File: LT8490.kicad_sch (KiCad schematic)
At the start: 81 parts

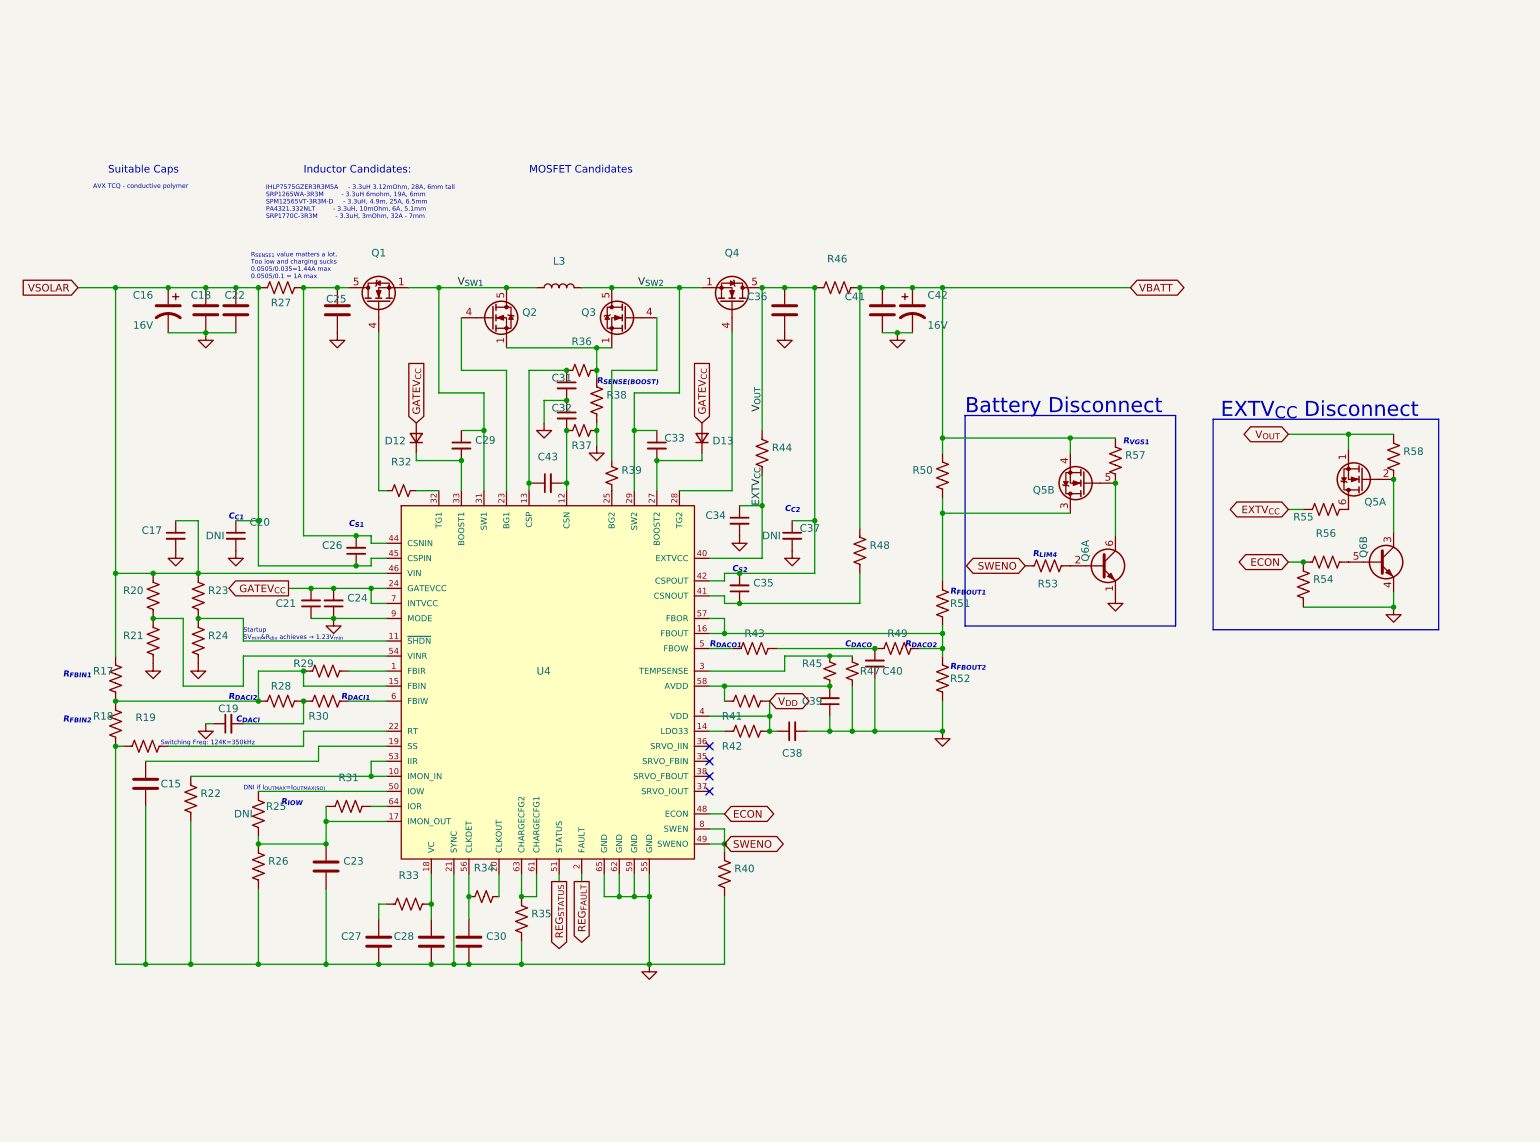
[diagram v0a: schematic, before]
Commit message: routed on 6 layers. Possible to do 4?
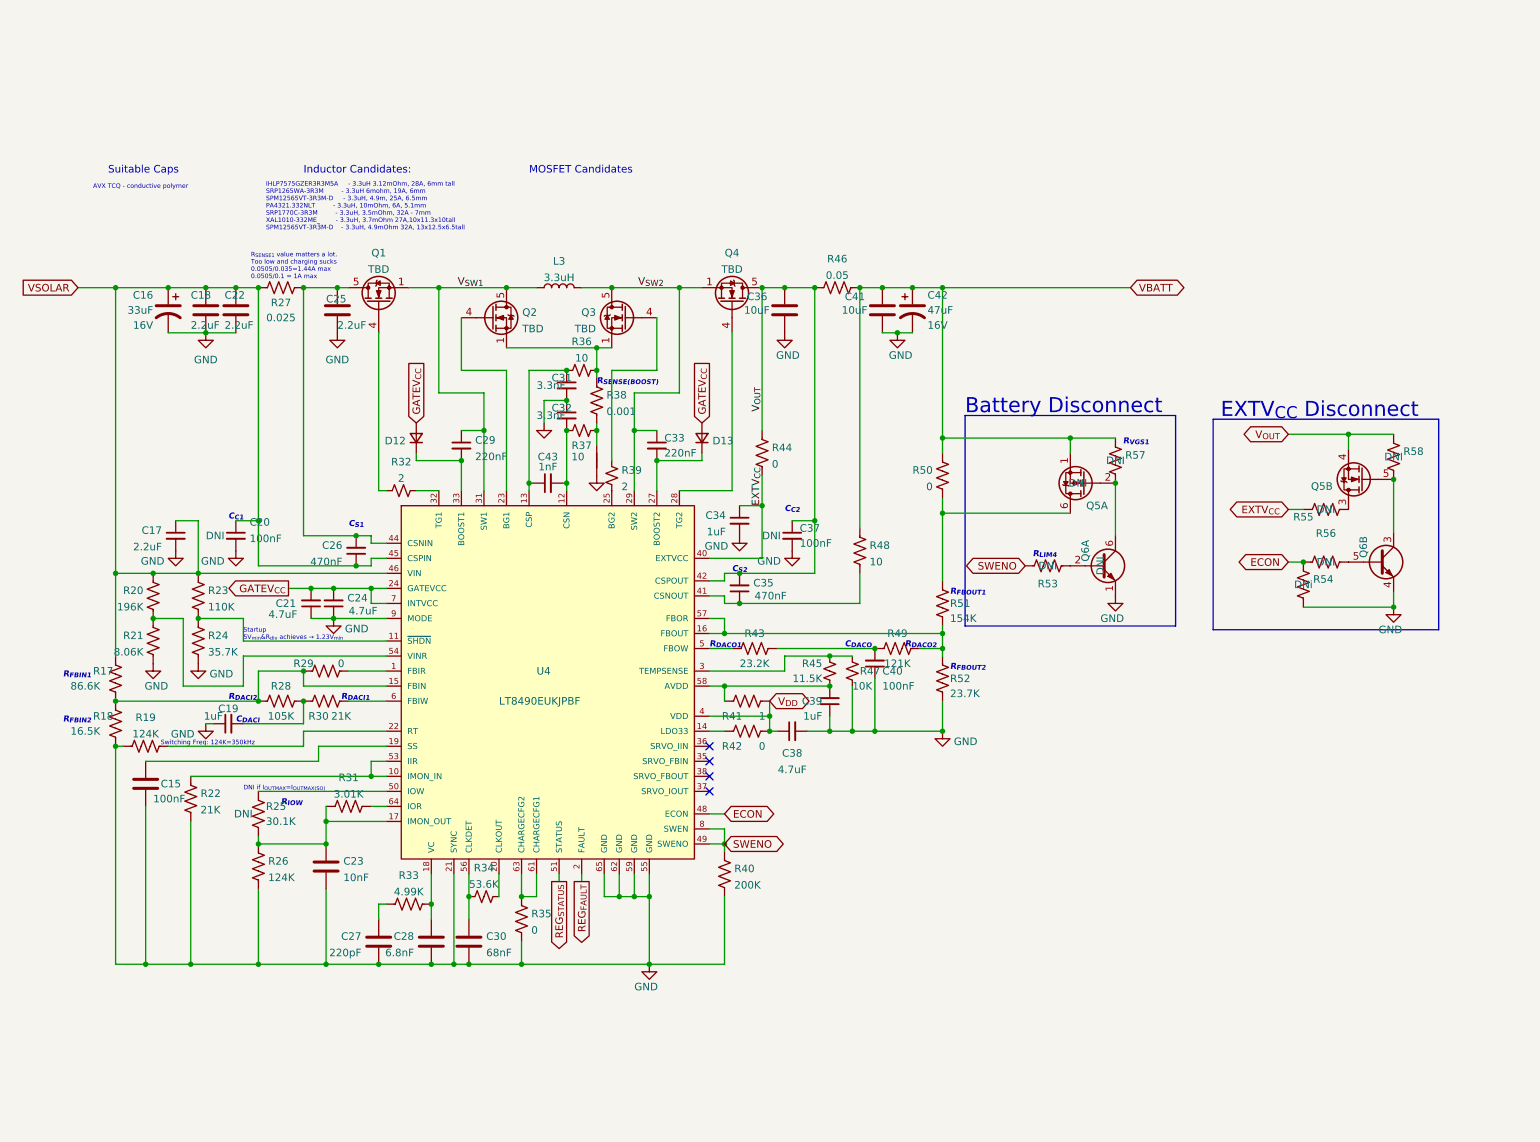
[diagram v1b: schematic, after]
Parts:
- added NT1: NetTie_2, NetTie:NetTie-2_SMD_Pad0.5mm, symbol Device:NetTie_2
- C15, C20, C37, C40: value (none) -> 100nF; footprint (none) -> Capacitor_SMD:C_0603_1608Metric
- C16: value (none) -> 33uF; footprint (none) -> Capacitor_Tantalum_SMD:CP_EIA-7343-30_AVX-N
- C17: value (none) -> 2.2uF; footprint (none) -> Capacitor_SMD:C_0603_1608Metric
- C18, C22, C25: value (none) -> 2.2uF; footprint (none) -> Capacitor_SMD:C_0805_2012Metric
- C19, C34, C39: value (none) -> 1uF; footprint (none) -> Capacitor_SMD:C_0603_1608Metric
- C21, C24, C38: value (none) -> 4.7uF; footprint (none) -> Capacitor_SMD:C_0603_1608Metric
- C23: value (none) -> 10nF; footprint (none) -> Capacitor_SMD:C_0603_1608Metric
- C26, C35: value (none) -> 470nF; footprint (none) -> Capacitor_SMD:C_0603_1608Metric
- C27: value (none) -> 220pF; footprint (none) -> Capacitor_SMD:C_0603_1608Metric
- C28: value (none) -> 6.8nF; footprint (none) -> Capacitor_SMD:C_0603_1608Metric
- C29, C33: value (none) -> 220nF; footprint (none) -> Capacitor_SMD:C_0603_1608Metric
- C30: value (none) -> 68nF; footprint (none) -> Capacitor_SMD:C_0603_1608Metric
- C31, C32: value (none) -> 3.3nF; footprint (none) -> Capacitor_SMD:C_0603_1608Metric
- C36, C41: value (none) -> 10uF; footprint (none) -> Capacitor_SMD:C_0805_2012Metric
- C42: value (none) -> 47uF; footprint (none) -> Capacitor_Tantalum_SMD:CP_EIA-7343-30_AVX-N
- C43: value (none) -> 1nF; footprint (none) -> Capacitor_SMD:C_0603_1608Metric
- D12, D13: value (none) -> DFLS130L; footprint (none) -> Diode_SMD:D_PowerDI-123
- L3: value (none) -> 3.3uH; footprint (none) -> custom-footprints:L_IHLP7575
- Q1, Q2, Q3, Q4: value (none) -> TBD; footprint (none) -> Package_SO:PowerPAK_SO-8_Single
- Q5, Q6, R53, R55, R56, R57, R58: DNI (none) -> DNI
- R17: value (none) -> 86.6K; footprint (none) -> Resistor_SMD:R_0603_1608Metric
- R18: value (none) -> 16.5K; footprint (none) -> Resistor_SMD:R_0603_1608Metric
- R19, R26: value (none) -> 124K; footprint (none) -> Resistor_SMD:R_0603_1608Metric
- R20: value (none) -> 196K; footprint (none) -> Resistor_SMD:R_0603_1608Metric
- R21: value (none) -> 8.06K; footprint (none) -> Resistor_SMD:R_0603_1608Metric
- R22, R30: value (none) -> 21K; footprint (none) -> Resistor_SMD:R_0603_1608Metric
- R23: value (none) -> 110K; footprint (none) -> Resistor_SMD:R_0603_1608Metric
- R24: value (none) -> 35.7K; footprint (none) -> Resistor_SMD:R_0603_1608Metric
- R25: value (none) -> 30.1K; footprint (none) -> Resistor_SMD:R_0603_1608Metric
- R27: value (none) -> 0.025; footprint (none) -> Resistor_SMD:R_1206_3216Metric
- R28: value (none) -> 105K; footprint (none) -> Resistor_SMD:R_0603_1608Metric
- R29, R35, R42, R44, R50: value (none) -> 0; footprint (none) -> Resistor_SMD:R_0603_1608Metric
- R31: value (none) -> 3.01K; footprint (none) -> Resistor_SMD:R_0603_1608Metric
- R32, R39: value (none) -> 2; footprint (none) -> Resistor_SMD:R_0603_1608Metric
- R33: value (none) -> 4.99K; footprint (none) -> Resistor_SMD:R_0603_1608Metric
- R34: value (none) -> 53.6K; footprint (none) -> Resistor_SMD:R_0603_1608Metric
- R36, R37, R48: value (none) -> 10; footprint (none) -> Resistor_SMD:R_0603_1608Metric
- R38: value (none) -> 0.001; footprint (none) -> Resistor_SMD:R_1206_3216Metric
- R40: value (none) -> 200K; footprint (none) -> Resistor_SMD:R_0603_1608Metric
- R41: value (none) -> 1; footprint (none) -> Resistor_SMD:R_0603_1608Metric
- R43: value (none) -> 23.2K; footprint (none) -> Resistor_SMD:R_0603_1608Metric
- R45: value (none) -> 11.5K; footprint (none) -> Resistor_SMD:R_0603_1608Metric
- R46: value (none) -> 0.05; footprint (none) -> Resistor_SMD:R_1206_3216Metric
- R47: value (none) -> 10K; footprint (none) -> Resistor_SMD:R_0603_1608Metric
- R49: value (none) -> 121K; footprint (none) -> Resistor_SMD:R_0603_1608Metric
- R51: value (none) -> 154K; footprint (none) -> Resistor_SMD:R_0603_1608Metric
- R52: value (none) -> 23.7K; footprint (none) -> Resistor_SMD:R_0603_1608Metric
- R54: DNI (none) -> DNi
- U4: value (none) -> LT8490EUKJPBF; footprint (none) -> custom-footprints:LT8490EUKJ#PBF
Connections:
- net GND: now also NT1.1; no longer R37.1, R38.2
- net VBATT: now also Q5.1 (S2); no longer Q5.4 (S1)
- net V_{OUT}: now also Q5.4 (S1); no longer Q5.1 (S2)
- net at Q6.3 (C2), R58.1: now also Q5.5 (G1); no longer Q5.2 (G2)
- net at R50.2, R51.1: now also Q5.6 (D1); no longer Q5.3 (D2)
- net at R55.1: now also Q5.3 (D2); no longer Q5.6 (D1)
- net at Q6.6 (C1), R57.1: now also Q5.2 (G2); no longer Q5.5 (G1)
- new net: NT1.2, R37.1, R38.2
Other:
- note added: "IHLP7575GZER3R3M5A - 3.3uH 3.12mOhm, 28A, 6mm tall SRP1265WA-3R3M - 3.3uH 6mohm, 19A, 6mm SPM12565VT-3R3M-D - 3.3uH, 4.9m, 25A, 6.5mm PA4321.332NLT - 3.3uH, 10mOhm, 6A, 5.1mm SRP1770C-3R3M - 3.3uH, 3.5mOhm, 32A - 7mm XAL1010-332ME_ - 3.3uH, 3.7mOhm 27A,10x11.3x10tall SPM12565VT-3R3M-D - 3.3uH, 4.9mOhm 32A, 13x12.5x6.5tall"
- note removed: "IHLP7575GZER3R3M5A - 3.3uH 3.12mOhm, 28A, 6mm tall SRP1265WA-3R3M - 3.3uH 6mohm, 19A, 6mm SPM12565VT-3R3M-D - 3.3uH, 4.9m, 25A, 6.5mm PA4321.332NLT - 3.3uH, 10mOhm, 6A, 5.1mm SRP1770C-3R3M - 3.3uH, 3mOhm, 32A - 7mm"
- moved on the sheet: Q5A, Q5B

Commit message: evaluating layout for sensitive signals
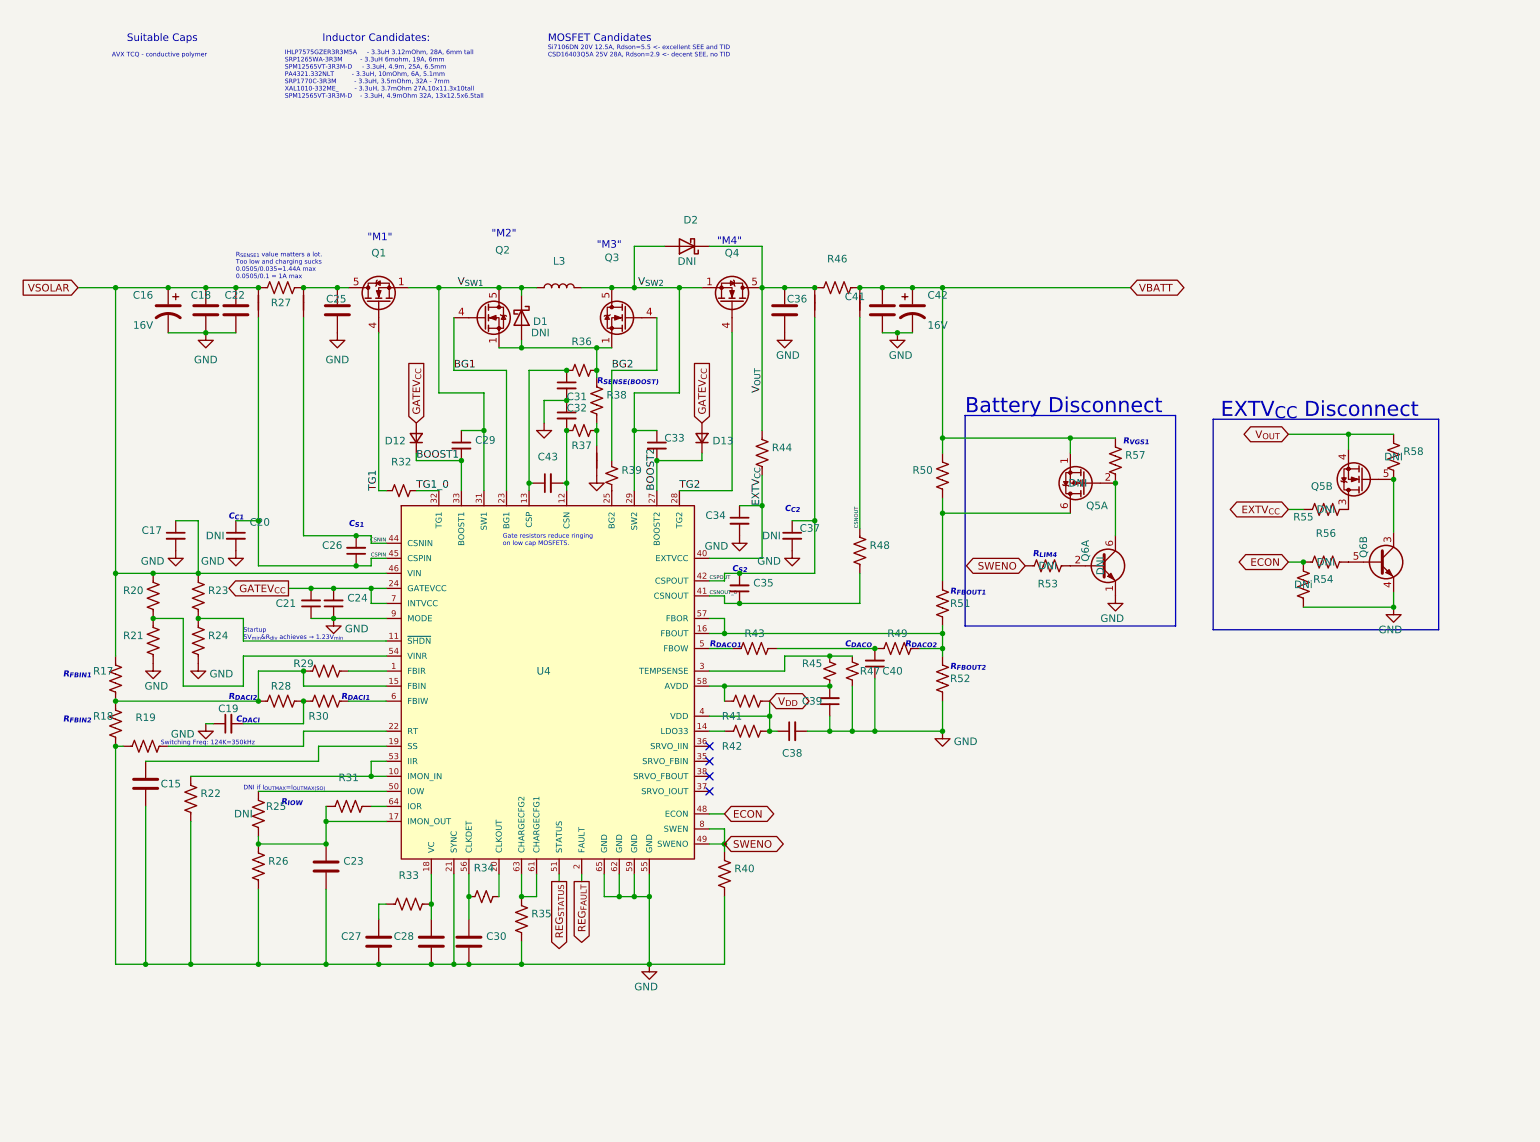
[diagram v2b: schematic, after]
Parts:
- added D1, D2: (no value), symbol Device:D_Schottky
- added NT2, NT3, NT4, NT5: NetTie_2, NetTie:NetTie-2_SMD_Pad0.5mm, symbol Device:NetTie_2
- C15, C20, C37, C40: value 100nF -> (none); footprint Capacitor_SMD:C_0603_1608Metric -> (none)
- C16: value 33uF -> (none); footprint Capacitor_Tantalum_SMD:CP_EIA-7343-30_AVX-N -> (none)
- C17: value 2.2uF -> (none); footprint Capacitor_SMD:C_0603_1608Metric -> (none)
- C18, C22, C25: value 2.2uF -> (none); footprint Capacitor_SMD:C_0805_2012Metric -> (none)
- C19, C34, C39: value 1uF -> (none); footprint Capacitor_SMD:C_0603_1608Metric -> (none)
- C21, C24, C38: value 4.7uF -> (none); footprint Capacitor_SMD:C_0603_1608Metric -> (none)
- C23: value 10nF -> (none); footprint Capacitor_SMD:C_0603_1608Metric -> (none)
- C26, C35: value 470nF -> (none); footprint Capacitor_SMD:C_0603_1608Metric -> (none)
- C27: value 220pF -> (none); footprint Capacitor_SMD:C_0603_1608Metric -> (none)
- C28: value 6.8nF -> (none); footprint Capacitor_SMD:C_0603_1608Metric -> (none)
- C29, C33: value 220nF -> (none); footprint Capacitor_SMD:C_0603_1608Metric -> (none)
- C30: value 68nF -> (none); footprint Capacitor_SMD:C_0603_1608Metric -> (none)
- C31, C32: value 3.3nF -> (none); footprint Capacitor_SMD:C_0603_1608Metric -> (none)
- C36, C41: value 10uF -> (none); footprint Capacitor_SMD:C_0805_2012Metric -> (none)
- C42: value 47uF -> (none); footprint Capacitor_Tantalum_SMD:CP_EIA-7343-30_AVX-N -> (none)
- C43: value 1nF -> (none); footprint Capacitor_SMD:C_0603_1608Metric -> (none)
- D12, D13: value DFLS130L -> (none); footprint Diode_SMD:D_PowerDI-123 -> (none)
- L3: value 3.3uH -> (none); footprint custom-footprints:L_IHLP7575 -> (none)
- NT1: value NetTie_2 -> (none); footprint NetTie:NetTie-2_SMD_Pad0.5mm -> (none)
- Q1, Q2, Q3, Q4: value TBD -> (none); footprint Package_SO:PowerPAK_SO-8_Single -> (none)
- R17: value 86.6K -> (none); footprint Resistor_SMD:R_0603_1608Metric -> (none)
- R18: value 16.5K -> (none); footprint Resistor_SMD:R_0603_1608Metric -> (none)
- R19, R26: value 124K -> (none); footprint Resistor_SMD:R_0603_1608Metric -> (none)
- R20: value 196K -> (none); footprint Resistor_SMD:R_0603_1608Metric -> (none)
- R21: value 8.06K -> (none); footprint Resistor_SMD:R_0603_1608Metric -> (none)
- R22, R30: value 21K -> (none); footprint Resistor_SMD:R_0603_1608Metric -> (none)
- R23: value 110K -> (none); footprint Resistor_SMD:R_0603_1608Metric -> (none)
- R24: value 35.7K -> (none); footprint Resistor_SMD:R_0603_1608Metric -> (none)
- R25: value 30.1K -> (none); footprint Resistor_SMD:R_0603_1608Metric -> (none)
- R27: value 0.025 -> (none); footprint Resistor_SMD:R_1206_3216Metric -> (none)
- R28: value 105K -> (none); footprint Resistor_SMD:R_0603_1608Metric -> (none)
- R29, R35, R42, R44, R50: value 0 -> (none); footprint Resistor_SMD:R_0603_1608Metric -> (none)
- R31: value 3.01K -> (none); footprint Resistor_SMD:R_0603_1608Metric -> (none)
- R32, R39: value 2 -> (none); footprint Resistor_SMD:R_0603_1608Metric -> (none)
- R33: value 4.99K -> (none); footprint Resistor_SMD:R_0603_1608Metric -> (none)
- R34: value 53.6K -> (none); footprint Resistor_SMD:R_0603_1608Metric -> (none)
- R36, R37, R48: value 10 -> (none); footprint Resistor_SMD:R_0603_1608Metric -> (none)
- R38: value 0.001 -> (none); footprint Resistor_SMD:R_1206_3216Metric -> (none)
- R40: value 200K -> (none); footprint Resistor_SMD:R_0603_1608Metric -> (none)
- R41: value 1 -> (none); footprint Resistor_SMD:R_0603_1608Metric -> (none)
- R43: value 23.2K -> (none); footprint Resistor_SMD:R_0603_1608Metric -> (none)
- R45: value 11.5K -> (none); footprint Resistor_SMD:R_0603_1608Metric -> (none)
- R46: value 0.05 -> (none); footprint Resistor_SMD:R_1206_3216Metric -> (none)
- R47: value 10K -> (none); footprint Resistor_SMD:R_0603_1608Metric -> (none)
- R49: value 121K -> (none); footprint Resistor_SMD:R_0603_1608Metric -> (none)
- R51: value 154K -> (none); footprint Resistor_SMD:R_0603_1608Metric -> (none)
- R52: value 23.7K -> (none); footprint Resistor_SMD:R_0603_1608Metric -> (none)
- U4: value LT8490EUKJPBF -> (none); footprint custom-footprints:LT8490EUKJ#PBF -> (none)
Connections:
- net VBATT: now also NT5.2; no longer R48.1
- net VSOLAR: now also NT2.2; no longer C20.1, C26.1, U4.45 (CSPIN)
- net V_{OUT}: now also D2.1 (K), NT4.2; no longer C35.2, C37.1, U4.42 (CSPOUT)
- net V_{SW1}: now also D1.1 (K)
- net V_{SW2}: now also D2.2 (A)
- net at C25.1, Q1.5 (D), R27.2: now also NT3.2; no longer C26.2, U4.44 (CSNIN)
- net at Q2.1 (S), Q2.2 (S), Q2.3 (S)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: now also D1.2 (A)
- net BG2: now reaches Q3.4 (G), R39.1
- net BOOST1: now reaches C29.2, D12.1 (K), U4.33 (BOOST1)
- net BG1: now reaches Q2.4 (G), U4.23 (BG1)
- net BOOST2: now reaches C33.2, D13.1 (K), U4.27 (BOOST2)
- net TG2: now reaches Q4.4 (G), U4.28 (TG2)
- net TG1_0: now reaches R32.1, U4.32 (TG1)
- net CSNOUT_0: now reaches C35.1, R48.2, U4.41 (CSNOUT)
- net TG1: now reaches Q1.4 (G), R32.2
- new net CSNIN: C26.2, NT3.1, U4.44 (CSNIN)
- new net CSNOUT: NT5.1, R48.1
- new net CSPIN: C20.1, C26.1, NT2.1, U4.45 (CSPIN)
- new net CSPOUT: C35.2, C37.1, NT4.1, U4.42 (CSPOUT)
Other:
- note added: ""M1""
- note added: ""M2""
- note added: ""M3""
- note added: ""M4""
- note added: "Gate resistors reduce ringing on low cap MOSFETS."
- note added: "Si7106DN 20V 12.5A, Rdson=5.5 <- excellent SEE and TID CSD16403Q5A 25V 28A, Rdson=2.9 <- decent SEE, no TID"
- moved on the sheet: Q2
